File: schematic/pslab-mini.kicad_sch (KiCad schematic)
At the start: 182 parts, among them J1 USB_C_Receptacle_USB2.0_16P, J2 BAT, J3 Conn_Coaxial, J4 Conn_Coaxial, J5 Conn_02x16_Odd_Even, J6 Conn_01x15_Socket, J7 Conn_02x03_Top_Bottom, Q1 MMBT3904, Q2 MMBT3904, SW1 Reset, SW4 Power, U1 AMS1117-3.3, U10 OPA356AIDBVR, U11 ESP32-C3, U12 W25Q32JV, U2 MT2496, U3 IP5189T, U4 SP0503BAHT, U5 OPA356AIDBVR, U6 OPA356AIDBVR, U7 TLV9001IDCK, U8 STM32H563RIT6, U9 OPA356AIDBVR, X1 32kHz768, Y1 Crystal_25MHz, Y2 40MHz

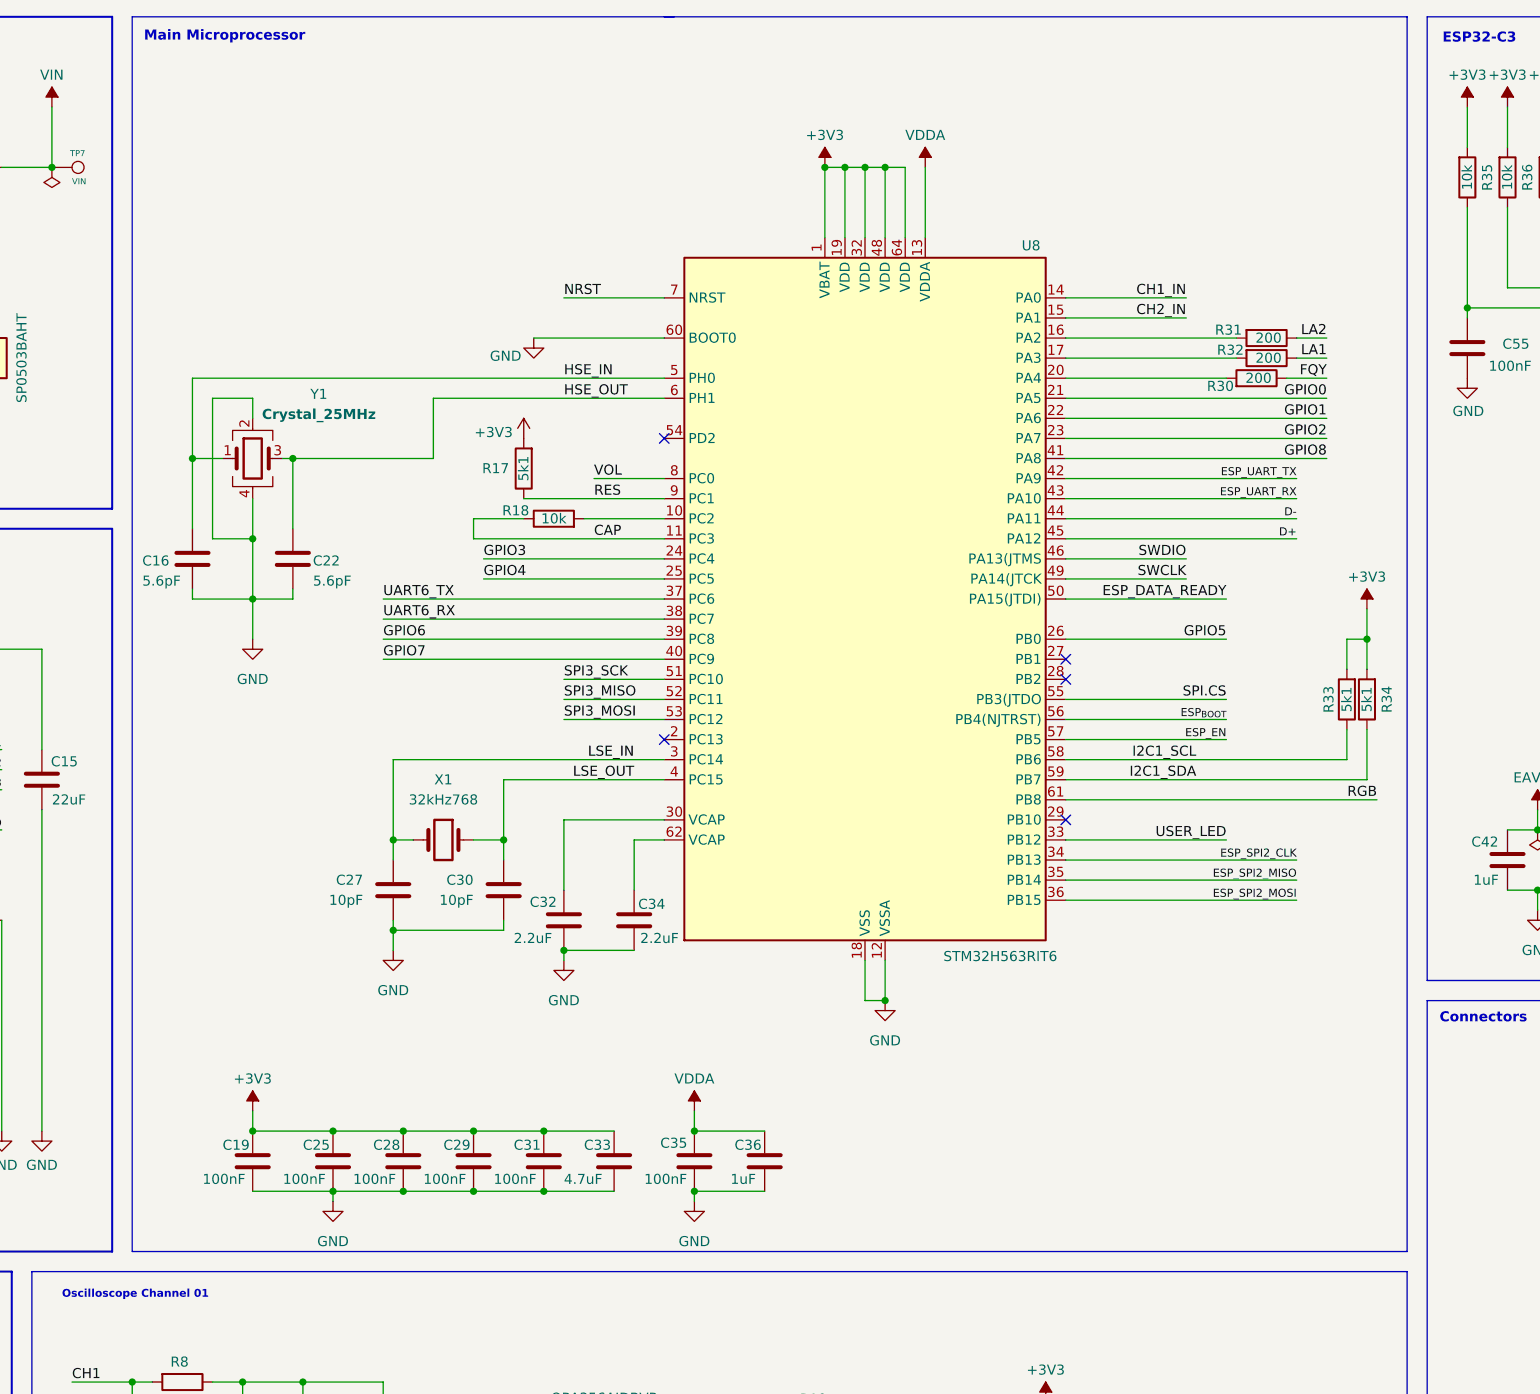
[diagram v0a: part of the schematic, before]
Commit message: feat: replaced the stm32 schematic with rp2350B
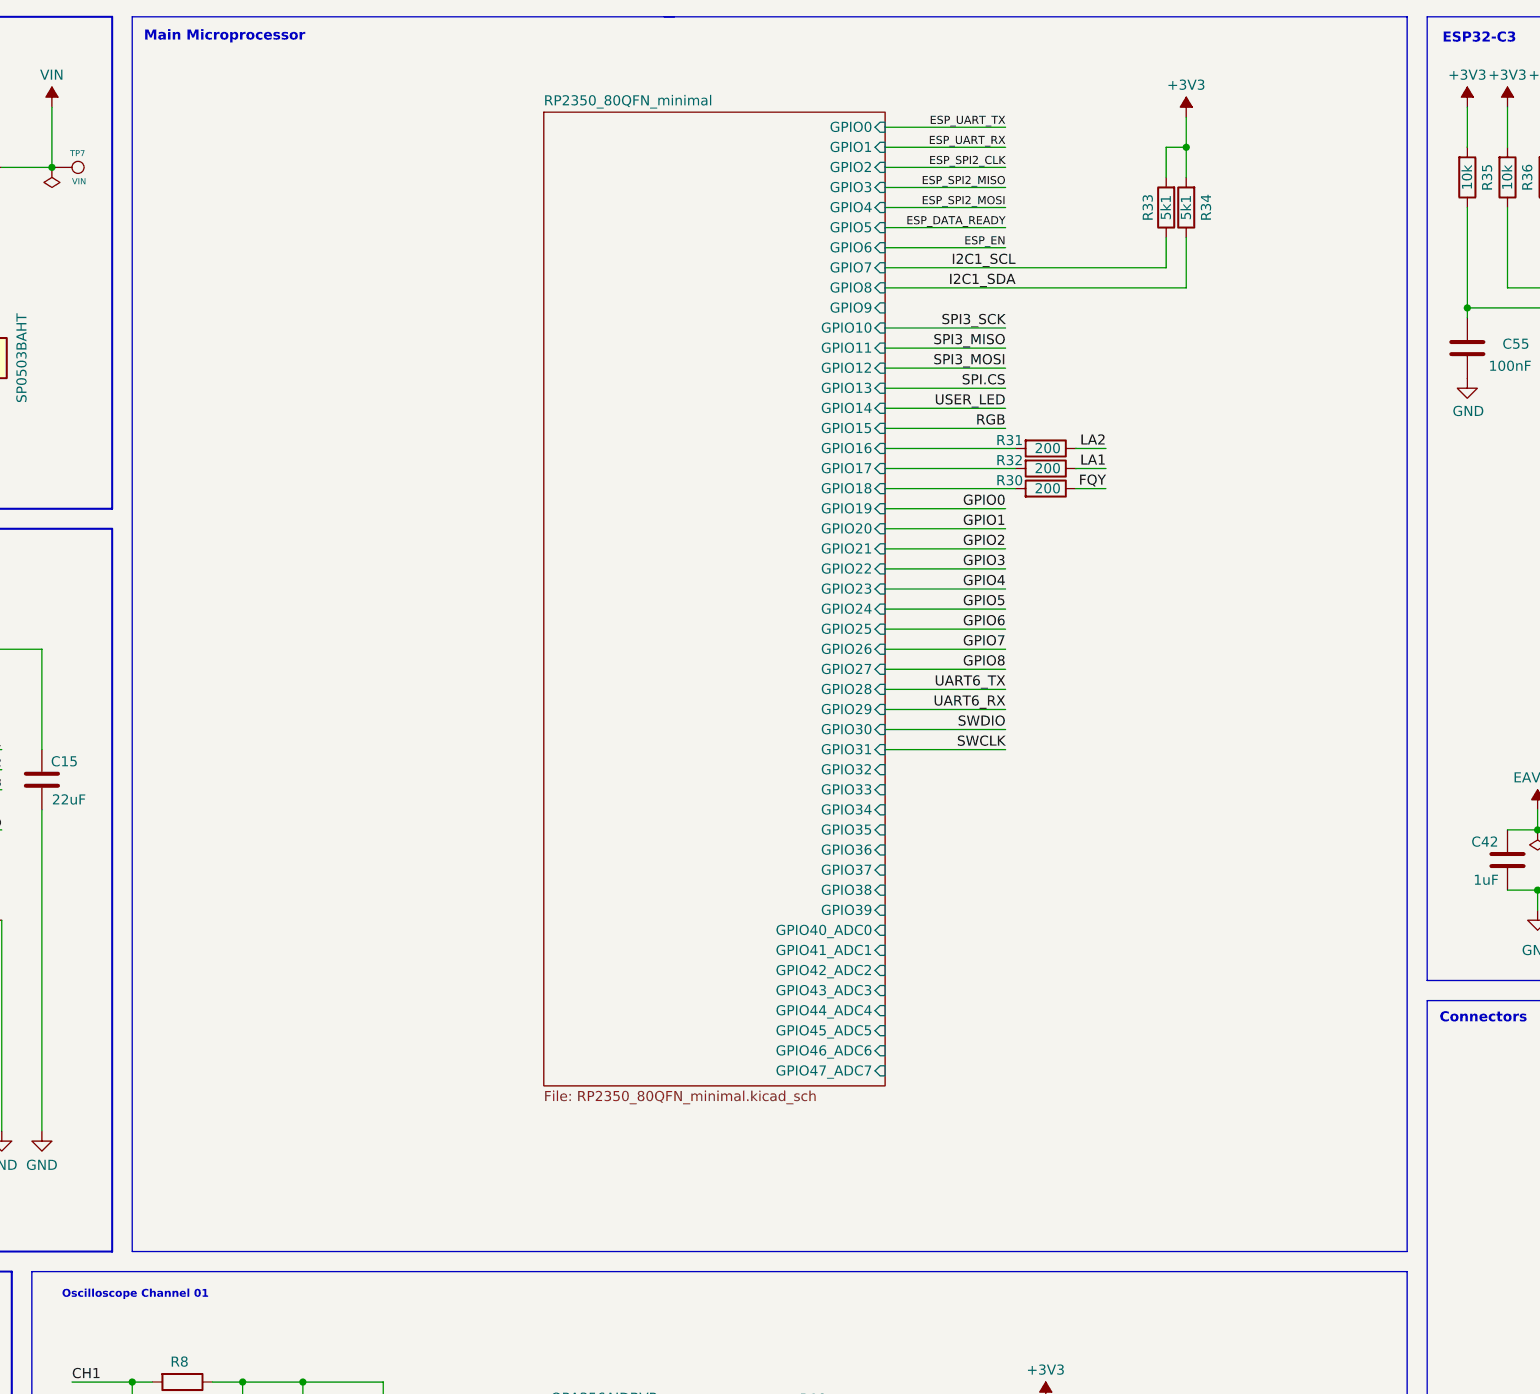
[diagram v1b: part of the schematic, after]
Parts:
- removed C16, C22: 5.6pF, Capacitor_SMD:C_0603_1608Metric, symbol Device:C
- removed C19, C25, C28, C29, C31, C35: 100nF, Capacitor_SMD:C_0603_1608Metric, symbol Device:C
- removed C27, C30: 10pF, Capacitor_SMD:C_0603_1608Metric, symbol Device:C
- removed C32, C34: 2.2uF, Capacitor_SMD:C_0805_2012Metric, symbol Device:C
- removed C33: 4.7uF, Capacitor_SMD:C_0805_2012Metric, symbol Device:C
- removed C36: 1uF, Capacitor_SMD:C_0603_1608Metric, symbol Device:C
- removed R17: 5k1, Resistor_SMD:R_0603_1608Metric, symbol Device:R
- removed R18: 10k, Resistor_SMD:R_0603_1608Metric, symbol Device:R
- removed U8: STM32H563RIT6, Package_QFP:LQFP-64_10x10mm_P0.5mm, symbol MCU_ST_STM32H5:STM32H563RITx
- removed X1: 32kHz768, Crystal:Crystal_SMD_3215-2Pin_3.2x1.5mm, symbol Device:Crystal
- removed Y1: Crystal_25MHz, Crystal:Crystal_SMD_3225-4Pin_3.2x2.5mm, symbol Device:Crystal_GND24
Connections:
- net RP2350_80QFN_minimal/GPIO16: now reaches R31.2
- net RP2350_80QFN_minimal/GPIO17: now reaches R32.2
- net RP2350_80QFN_minimal/GPIO18: now reaches R30.2
- no-connect marks 19 -> 14
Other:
- added sheet RP2350_80QFN_minimal (RP2350_80QFN_minimal.kicad_sch)
- moved on the sheet: R30, R31, R32, R33, R34

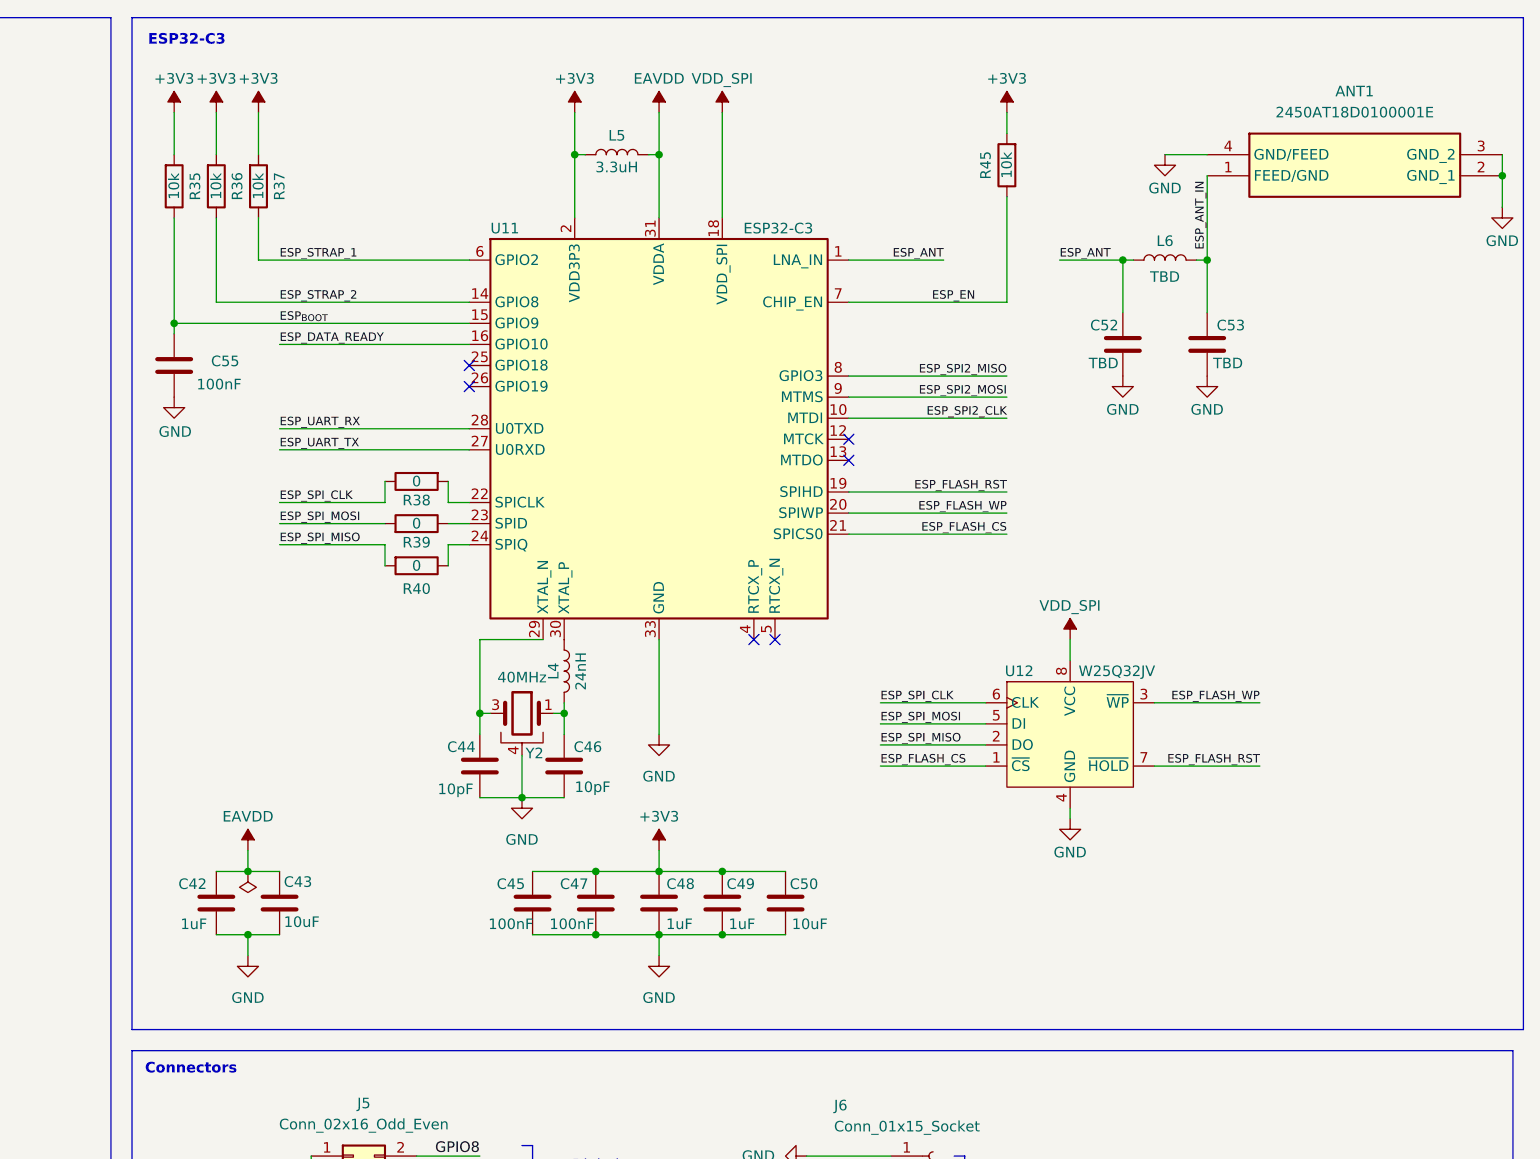
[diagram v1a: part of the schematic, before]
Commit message: feat: replace esp32-c3 ic schematic with esp32-c3 supermini module
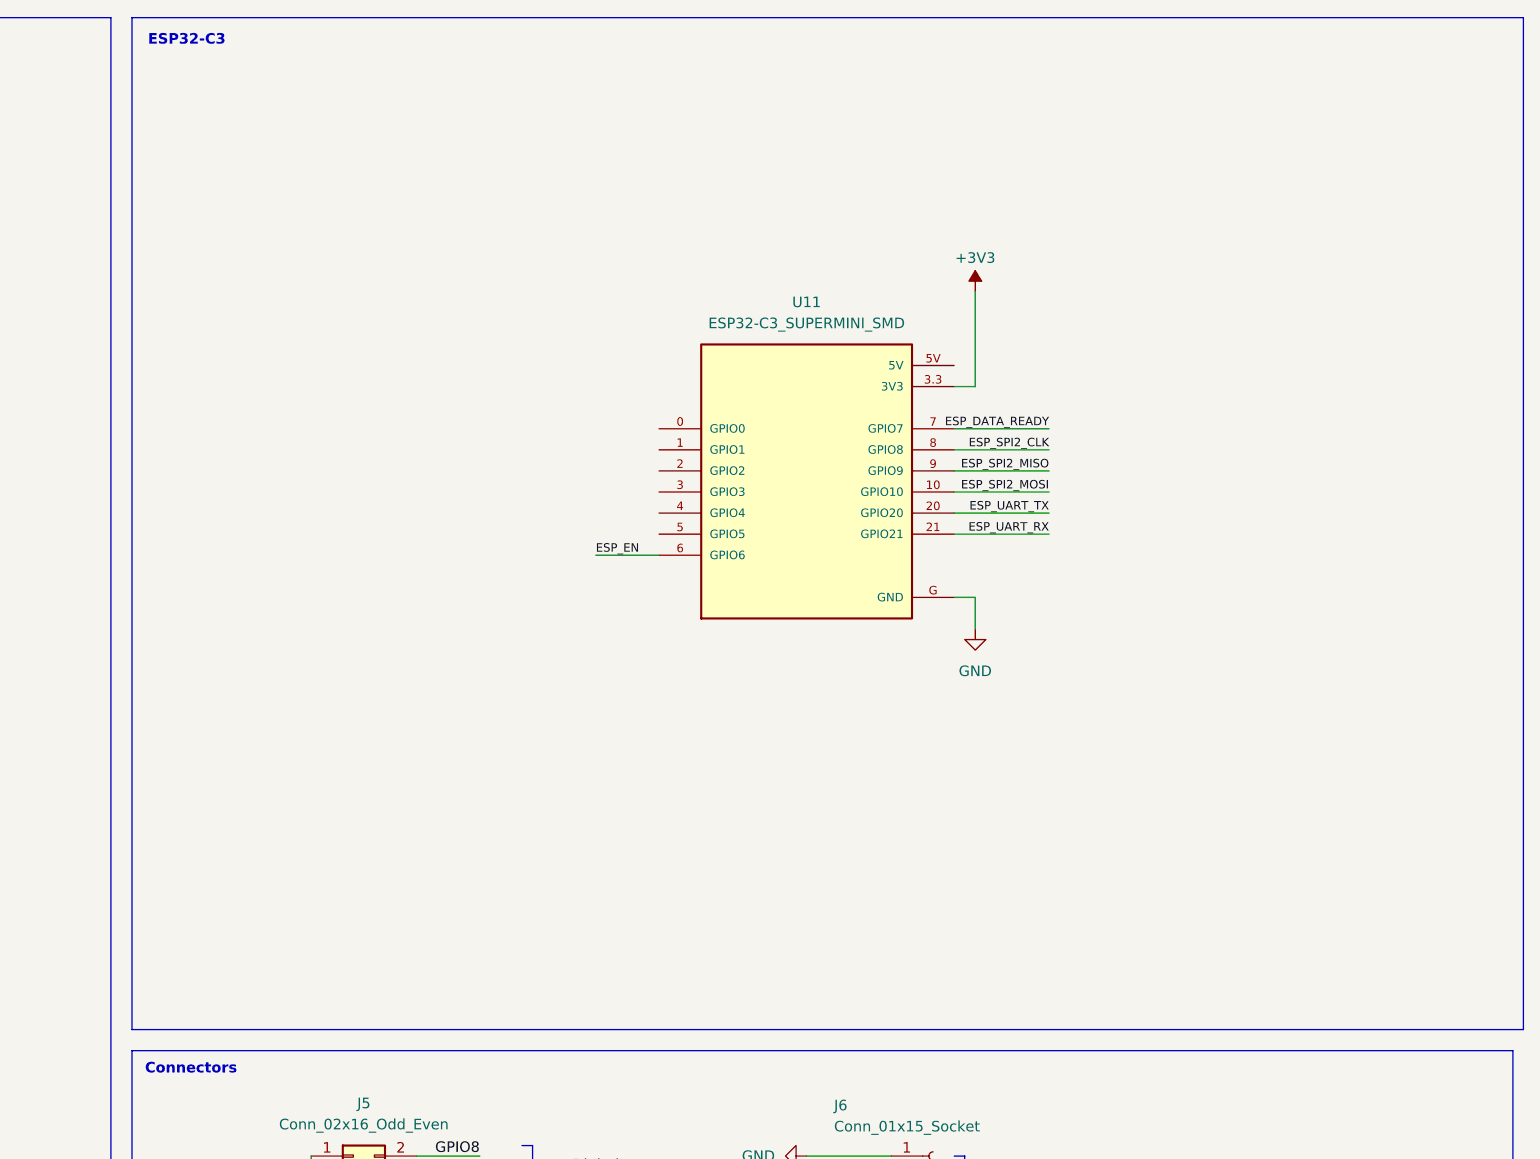
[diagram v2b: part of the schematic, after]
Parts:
- removed ANT1: 2450AT18D0100001E, pslab-mini:2450AT18D0100001E, symbol pslab-mini:2450AT18D0100001E
- removed C42, C48, C49: 1uF, Capacitor_SMD:C_0603_1608Metric, symbol Device:C
- removed C43, C50: 10uF, Capacitor_SMD:C_0805_2012Metric, symbol Device:C
- removed C44, C46: 10pF, Capacitor_SMD:C_0603_1608Metric, symbol Device:C
- removed C45, C47, C55: 100nF, Capacitor_SMD:C_0603_1608Metric, symbol Device:C
- removed C52, C53: TBD, Capacitor_SMD:C_0402_1005Metric, symbol Device:C
- removed L4: 24nH, Inductor_SMD:L_0402_1005Metric, symbol Device:L
- removed L5: 3.3uH, Inductor_SMD:L_0603_1608Metric, symbol Device:L
- removed L6: TBD, Inductor_SMD:L_0402_1005Metric, symbol Device:L
- removed R35, R36, R37, R45: 10k, Resistor_SMD:R_0603_1608Metric, symbol Device:R
- removed R38, R39, R40: 0, Resistor_SMD:R_0402_1005Metric, symbol Device:R
- removed U11: ESP32-C3, Package_DFN_QFN:QFN-32-1EP_5x5mm_P0.5mm_EP3.7x3.7mm, symbol pslab-mini:ESP32-C3
- removed U12: W25Q32JV, Package_SO:SOIC-8_5.3x5.3mm_P1.27mm, symbol pslab-mini:Flash_W25Q32JV
- removed Y2: 40MHz, Crystal:Crystal_SMD_3225-4Pin_3.2x2.5mm, symbol pslab-mini:Crystal_GND24
- added U11: ESP32-C3_SUPERMINI_SMD, ESP32-C3_SUPERMINI_SMD:MODULE_ESP32-C3_SUPERMINI, symbol ESP32-C3_SUPERMINI_SMD:ESP32-C3_SUPERMINI_SMD
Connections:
- net +3V3: now also U11.3.3 (3V3)
- net AGND: now also U11.G (GND)
- net ESP_DATA_READY: now also U11.7 (GPIO7)
- net ESP_EN: now also U11.6 (GPIO6)
- net ESP_SPI2_CLK: now also U11.8 (GPIO8)
- net ESP_SPI2_MISO: now also U11.9 (GPIO9)
- net ESP_SPI2_MOSI: now also U11.10 (GPIO10)
- net ESP_UART_RX: now also U11.21 (GPIO21)
- net ESP_UART_TX: now also U11.20 (GPIO20)
- no-connect marks 14 -> 8

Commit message: fix: the D+ and D- lines were unedited from the official rp2350B example schematic
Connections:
- net I2C1_SCL: no longer R33.1
- net I2C1_SDA: no longer R34.1
- new net RP2350_80QFN_minimal/GPIO7: R33.1
- new net RP2350_80QFN_minimal/GPIO8: R34.1
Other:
- added sheet adc-AD9629 (adc-AD9629.kicad_sch)
- sheet RP2350_80QFN_minimal ports: added D+, D-; removed none
- moved on the sheet: R30, R31, R32, R33, R34

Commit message: fix: organised the schematic a bit by moving AFE to it's own schematic sheet
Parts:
- removed C10, C13, C5, C51, C57, C58, C59: 100nF, Capacitor_SMD:C_0402_1005Metric, symbol Device:C
- removed C12: 12pF, Capacitor_SMD:C_0603_1608Metric, symbol Device:C
- removed C14, C4: 22uF, Capacitor_SMD:C_0805_2012Metric, symbol Device:C
- removed C17, C18: 2pF~6pF, pslab-mini:STC3MA06-T1, symbol Device:C_Trim
- removed C20, C23: 16pF, Capacitor_SMD:C_0603_1608Metric, symbol Device:C
- removed C21, C24: 90pF, Capacitor_SMD:C_0603_1608Metric, symbol Device:C
- removed C26: 10uF, Capacitor_SMD:C_0805_2012Metric, symbol Device:C
- removed C37: 100nF, Capacitor_SMD:C_0603_1608Metric, symbol Device:C
- removed C38, C39: 1.2pF, Capacitor_SMD:C_0603_1608Metric, symbol Device:C
- removed C40, C41: 22pF, Capacitor_SMD:C_0603_1608Metric, symbol Device:C
- removed C9: 22nF, Capacitor_SMD:C_0603_1608Metric, symbol Device:C
- removed GD1, GD2: SMD3216-090N, pslab-mini:SMD3216-090N, symbol pslab-mini:GDT_2Pin
- removed J3, J4: Conn_Coaxial, pslab-mini:BNC_connector_dosinconn DOSIN-801-0050, symbol Connector:Conn_Coaxial
- removed L3: 3.3uH, Inductor_SMD:L_0603_1608Metric, symbol Device:L
- removed R10, R12: 180k, Resistor_SMD:R_0603_1608Metric, symbol Device:R
- removed R11, R9: 820k, Resistor_SMD:R_0603_1608Metric, symbol Device:R
- removed R13, R16: 2k, Resistor_SMD:R_0603_1608Metric, symbol Device:R
- removed R14, R15, R19, R21, R26, R27: 10k, Resistor_SMD:R_0603_1608Metric, symbol Device:R
- removed R20, R22, R24, R25, R49, R50, R51, R52: 3k, Resistor_SMD:R_0402_1005Metric, symbol Device:R
- removed R23: 4R7, Resistor_SMD:R_0603_1608Metric, symbol Device:R
- removed R28, R29: 47R, Resistor_SMD:R_0603_1608Metric, symbol Device:R
- removed R3: 100k, Resistor_SMD:R_0603_1608Metric, symbol Device:R
- removed R4: 42.2k, Resistor_SMD:R_0603_1608Metric, symbol Device:R
- removed R7, R8: 10R, Resistor_SMD:R_0603_1608Metric, symbol Device:R
- removed TP6: -2V, pslab-mini:Test_Point_0.8mm, symbol Connector:TestPoint
- removed TP8: Vref, pslab-mini:Test_Point_0.8mm, symbol Connector:TestPoint
- removed U10, U5, U6, U9: OPA356AIDBVR, Package_TO_SOT_SMD:SOT-23-5, symbol pslab-mini:OPA356AIDBVR
- removed U2: MT2496, Package_TO_SOT_SMD:SOT-23-6, symbol pslab-mini:MT2496
- removed U7: TLV9001IDCK, Package_TO_SOT_SMD:SOT-353_SC-70-5, symbol Amplifier_Operational:TLV9001IDCK
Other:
- removed sheet adc-AD9629
- added sheet AFE (AFE.kicad_sch)
- note removed: "BNC Connectors"
- note removed: "Decoupling capacitor"
- note removed: "Decoupling capacitors"
- note removed: "Oscilloscope Channel 01"
- note removed: "Oscilloscope Channel 02"
- note removed: "V_{out} = 0.6 X [1 + R3/R4] = 2.02V"
- note removed: "Voltage Inverter"

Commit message: fix: removed unnecessary BJT reset button circuitry
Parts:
- removed C54, C56: 100nF, Capacitor_SMD:C_0603_1608Metric, symbol Device:C
- removed Q1, Q2: MMBT3904, pslab-mini:SOT-416, symbol Transistor_BJT:MMBT3904
- removed R46, R47, R48: 10k, Resistor_SMD:R_0603_1608Metric, symbol Device:R
- removed SW1: Reset, Button_Switch_SMD:SW_Tactile_SPST_NO_Straight_CK_PTS636Sx25SMTRLFS, symbol Switch:SW_Push
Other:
- note removed: "Reset Circuit"
- moved on the sheet: C11, C2, C8, D1, D2, D3, D4, D5, D6, D7, D8, FID1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
